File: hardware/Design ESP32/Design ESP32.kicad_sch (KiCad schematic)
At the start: 16 parts, among them J1 USB_C_Receptacle_USB2.0_16P, J2 Conn_01x08_Pin, U1 ESP32-S3-WROOM-1, U2 AMS1117-3.3

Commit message: edit skematik
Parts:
- added R5: R, symbol Device:R
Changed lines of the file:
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@@
+	(symbol
+		(lib_id "Device:R")
+		(at 57.15 109.22 0)
+		(unit 1)
+		(exclude_from_sim no)
+		(in_bom yes)
+		(on_board yes)
+		(dnp no)
+		(fields_autoplaced yes)
+		(property "Reference" "R5"
+			(at 59.69 107.9499 0)
+			(effects
+				(font
+					(size 1.27 1.27)
+				)
+				(justify left)
+			)
+		)
+		(property "Value" "R"
+			(at 59.69 110.4899 0)
+			(effects
+				(font
+					(size 1.27 1.27)
+				)
+				(justify left)
+			)
+		)
+		(property "Footprint" ""
+			(at 55.372 109.22 90)
+			(effects
+				(font
+					(size 1.27 1.27)
+				)
+				(hide yes)
+			)
+		)
+		(property "Datasheet" "~"
+			(at 57.15 109.22 0)
+			(effects
+				(font
+					(size 1.27 1.27)
+				)
+				(hide yes)
+			)
+		)
+		(property "Description" "Resistor"
+			(at 57.15 109.22 0)
+			(effects
+				(font
+					(size 1.27 1.27)
+				)
+				(hide yes)
+			)
+		)
+		(pin "1"
+		)
+		(pin "2"
+		)
+		(instances
+			(project ""
+				(path "/1962d16e-21fe-421b-a91f-5990a3b04182"
+					(reference "R5")
+					(unit 1)
+				)
+			)
+		)
+	)
 	(symbol
 		(lib_id "Device:R")

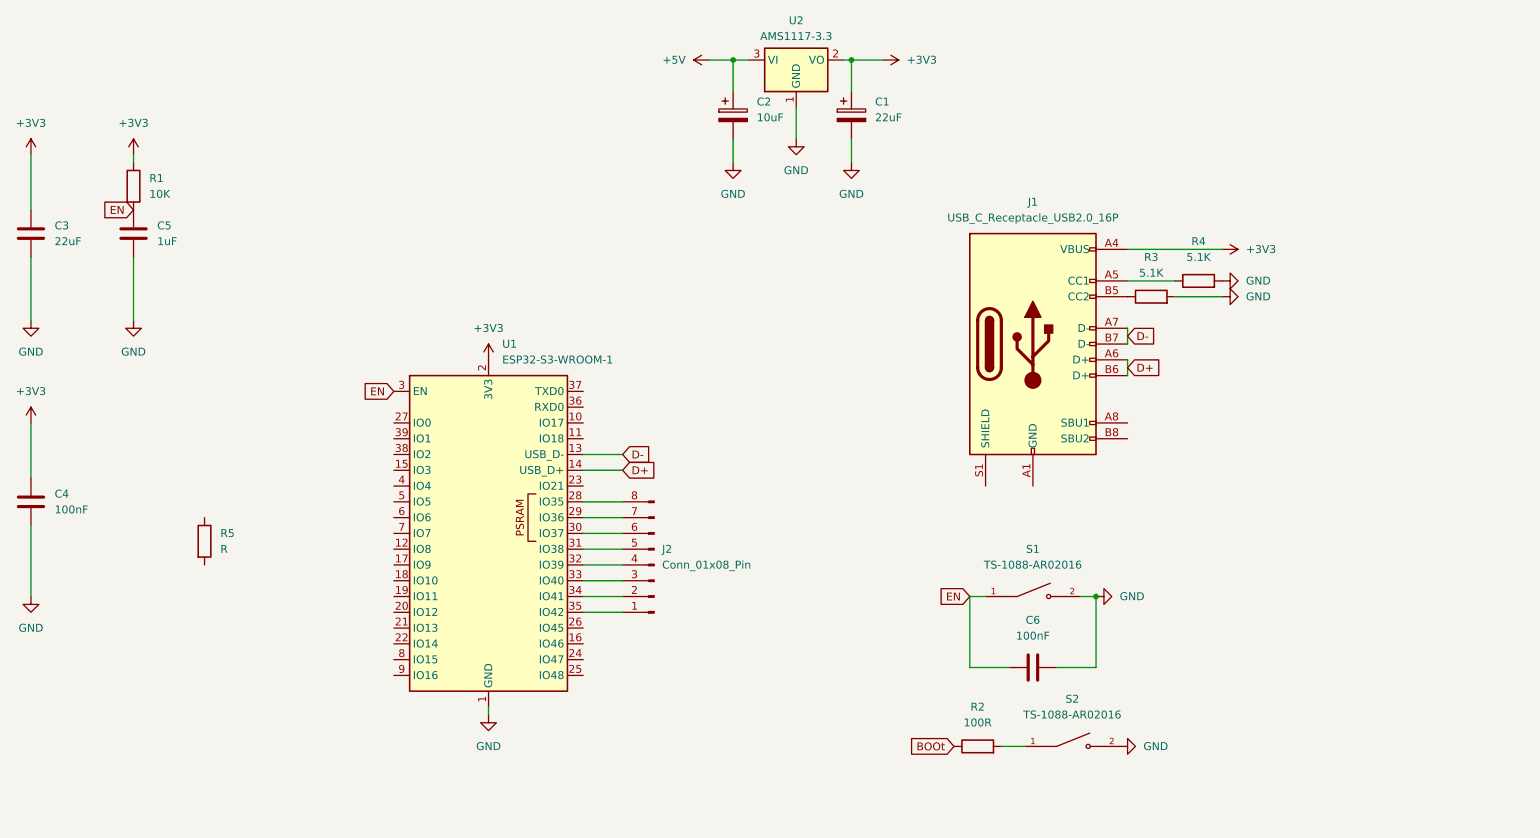
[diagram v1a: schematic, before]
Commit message: crosscheck schenmatic, progres track pcb
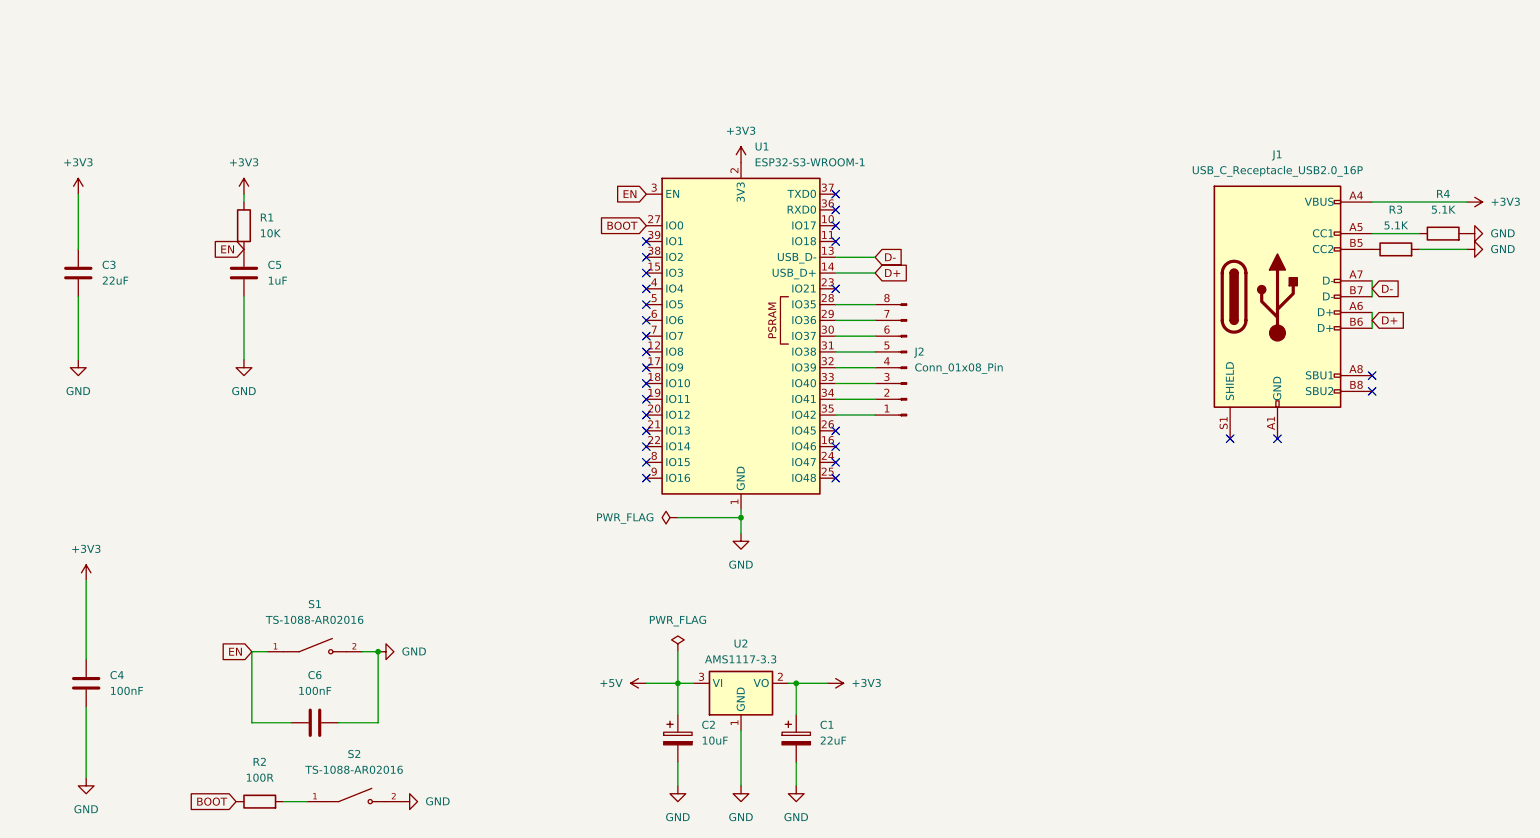
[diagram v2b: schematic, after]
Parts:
- removed R5: R, symbol Device:R
- C3, C4: footprint Capacitor_SMD:C_0805_2012Metric -> Capacitor_SMD:C_0603_1608Metric
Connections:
- net BOOt is gone; now on net BOOT: R2.1
- net BOOT: now reaches U1.27 (IO0)
- no-connect marks 0 -> 29
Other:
- moved on the sheet: C1, C2, C3, C4, C5, C6, J1, J2, R1, R2, R3, R4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

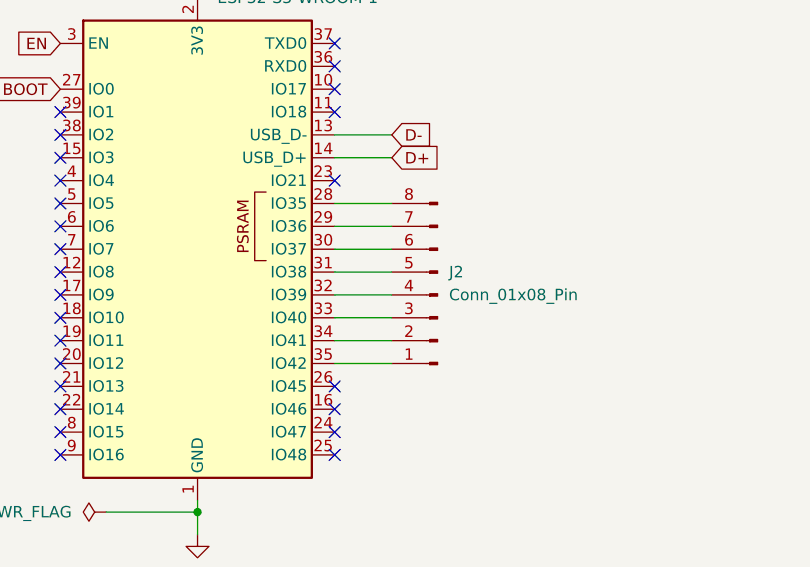
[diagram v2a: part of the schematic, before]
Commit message: jalur pcb, penanganan error 36 to 11
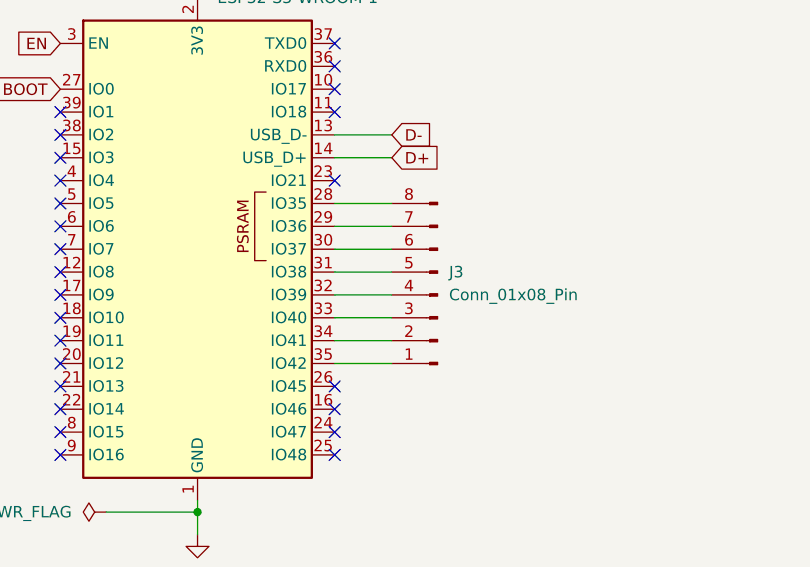
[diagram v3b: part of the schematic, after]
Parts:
- removed J2: Conn_01x08_Pin, Connector_PinHeader_1.00mm:PinHeader_1x08_P1.00mm_Vertical, symbol Connector:Conn_01x08_Pin
- added J3: Conn_01x08_Pin, Connector_PinHeader_1.00mm:PinHeader_1x08_P1.00mm_Vertical, symbol Connector:Conn_01x08_Pin
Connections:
- net at U1.35 (IO42): now also J3.1 (Pin_1)
- net at U1.34 (IO41): now also J3.2 (Pin_2)
- net at U1.33 (IO40): now also J3.3 (Pin_3)
- net at U1.32 (IO39): now also J3.4 (Pin_4)
- net at U1.31 (IO38): now also J3.5 (Pin_5)
- net at U1.30 (IO37): now also J3.6 (Pin_6)
- net at U1.29 (IO36): now also J3.7 (Pin_7)
- net at U1.28 (IO35): now also J3.8 (Pin_8)
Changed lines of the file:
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@@
-	(wire
-		(pts
-			(xy 165.1 86.36) (xy 158.75 86.36)
-		)
-		(stroke
-			(width 0)
-			(type default)
-		)
-	)
 	(wire
 		(pts
@@
 	(wire
 		(pts
+			(xy 158.75 88.9) (xy 165.1 88.9)
+		)
+		(stroke
+			(width 0)
+			(type default)
+		)
+	)
+	(wire
+		(pts
 			(xy 85.09 138.43) (xy 78.74 138.43)
 		)
@@
 	(wire
 		(pts
-			(xy 165.1 73.66) (xy 158.75 73.66)
+			(xy 158.75 73.66) (xy 165.1 73.66)
 		)
 		(stroke
@@
 	(wire
 		(pts
-			(xy 165.1 71.12) (xy 158.75 71.12)
-		)
-		(stroke
-			(width 0)
-			(type default)
-		)
-	)
-	(wire
-		(pts
 			(xy 143.51 139.7) (xy 143.51 148.59)
 		)
@@
 	(wire
 		(pts
+			(xy 158.75 76.2) (xy 165.1 76.2)
+		)
+		(stroke
+			(width 0)
+			(type default)
+		)
+	)
+	(wire
+		(pts
 			(xy 151.13 132.08) (xy 152.4 132.08)
 		)
@@
 	(wire
 		(pts
+			(xy 158.75 78.74) (xy 165.1 78.74)
+		)
+		(stroke
+			(width 0)
+			(type default)
+		)
+	)
+	(wire
+		(pts
 			(xy 38.1 147.32) (xy 38.1 135.89)
 		)
@@
 	(wire
 		(pts
-			(xy 165.1 81.28) (xy 158.75 81.28)
+			(xy 158.75 71.12) (xy 165.1 71.12)
 		)
 		(stroke
@@
 	(wire
 		(pts
+			(xy 158.75 83.82) (xy 165.1 83.82)
+		)
+		(stroke
+			(width 0)
+			(type default)
+		)
+	)
+	(wire
+		(pts
 			(xy 165.1 63.5) (xy 158.75 63.5)
 		)
@@
 	(wire
 		(pts
-			(xy 165.1 83.82) (xy 158.75 83.82)
-		)
-		(stroke
-			(width 0)
-			(type default)
-		)
-	)
-	(wire
-		(pts
 			(xy 67.31 127) (xy 64.77 127)
 		)
@@
 	(wire
 		(pts
-			(xy 165.1 88.9) (xy 158.75 88.9)
+			(xy 158.75 86.36) (xy 165.1 86.36)
+		)
+		(stroke
+			(width 0)
+			(type default)
+		)
+	)
+	(wire
+		(pts
+			(xy 158.75 81.28) (xy 165.1 81.28)
 		)
 		(stroke
@@
 		(pts
 			(xy 143.51 105.41) (xy 143.51 107.95)
-		)
-		(stroke
-			(width 0)
-			(type default)
-		)
-	)
-	(wire
-		(pts
-			(xy 165.1 78.74) (xy 158.75 78.74)
-		)
-		(stroke
-			(width 0)
-			(type default)
-		)
-	)
-	(wire
-		(pts
-			(xy 165.1 76.2) (xy 158.75 76.2)
 		)
 		(stroke
@@
 		(dnp no)
 		(fields_autoplaced yes)
-		(property "Reference" "J2"
+		(property "Reference" "J3"
 			(at 171.45 78.7399 0)
 			(effects
@@
 		)
 		(instances
-			(project ""
+			(project "Design ESP32"
 				(path "/1962d16e-21fe-421b-a91f-5990a3b04182"
-					(reference "J2")
+					(reference "J3")
 					(unit 1)
 				)

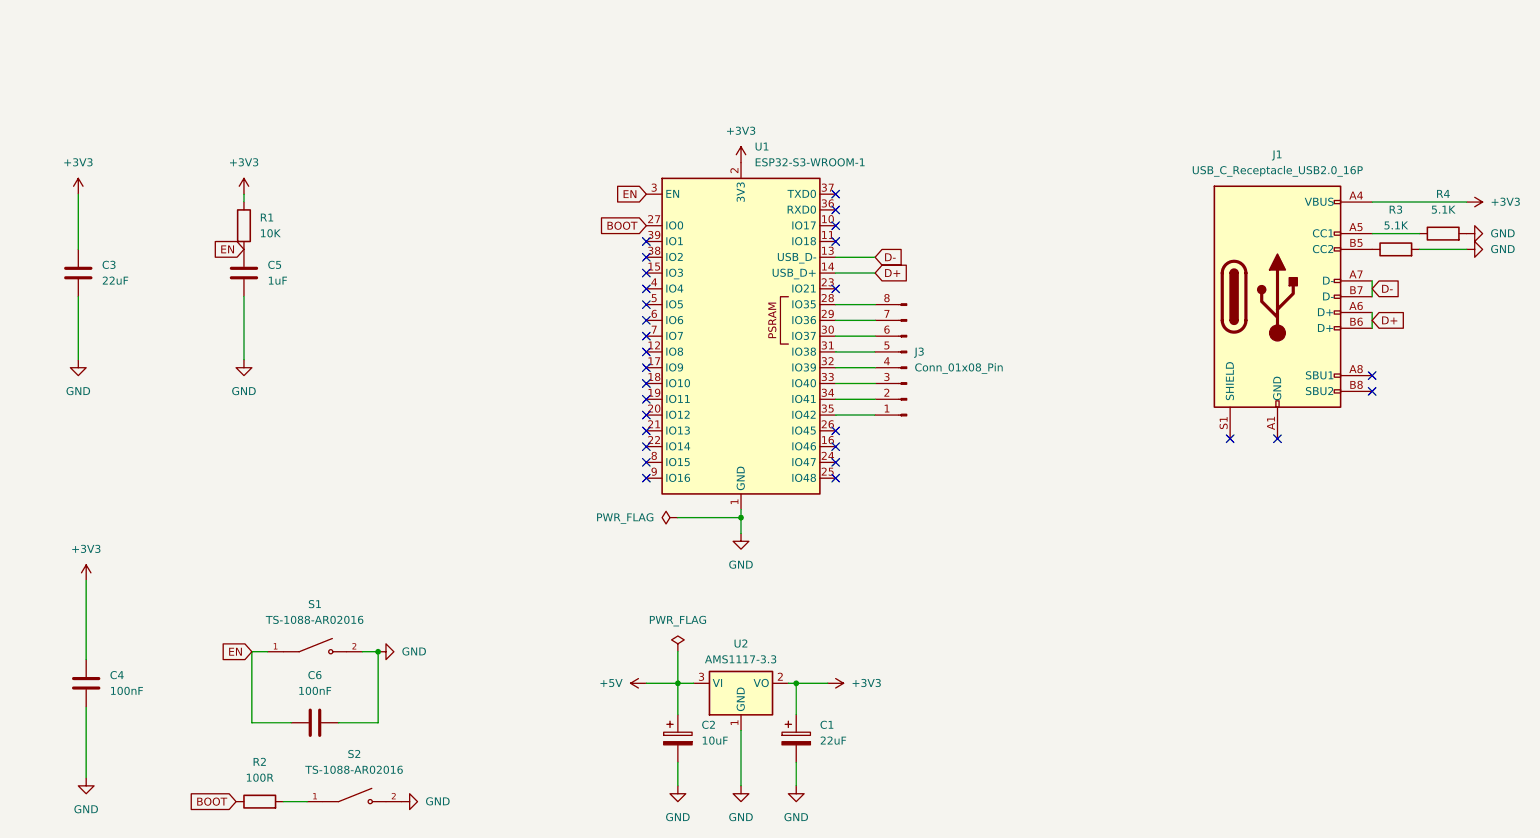
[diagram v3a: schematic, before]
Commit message: lanjut penanganan error dan penyelesaian design ESP32
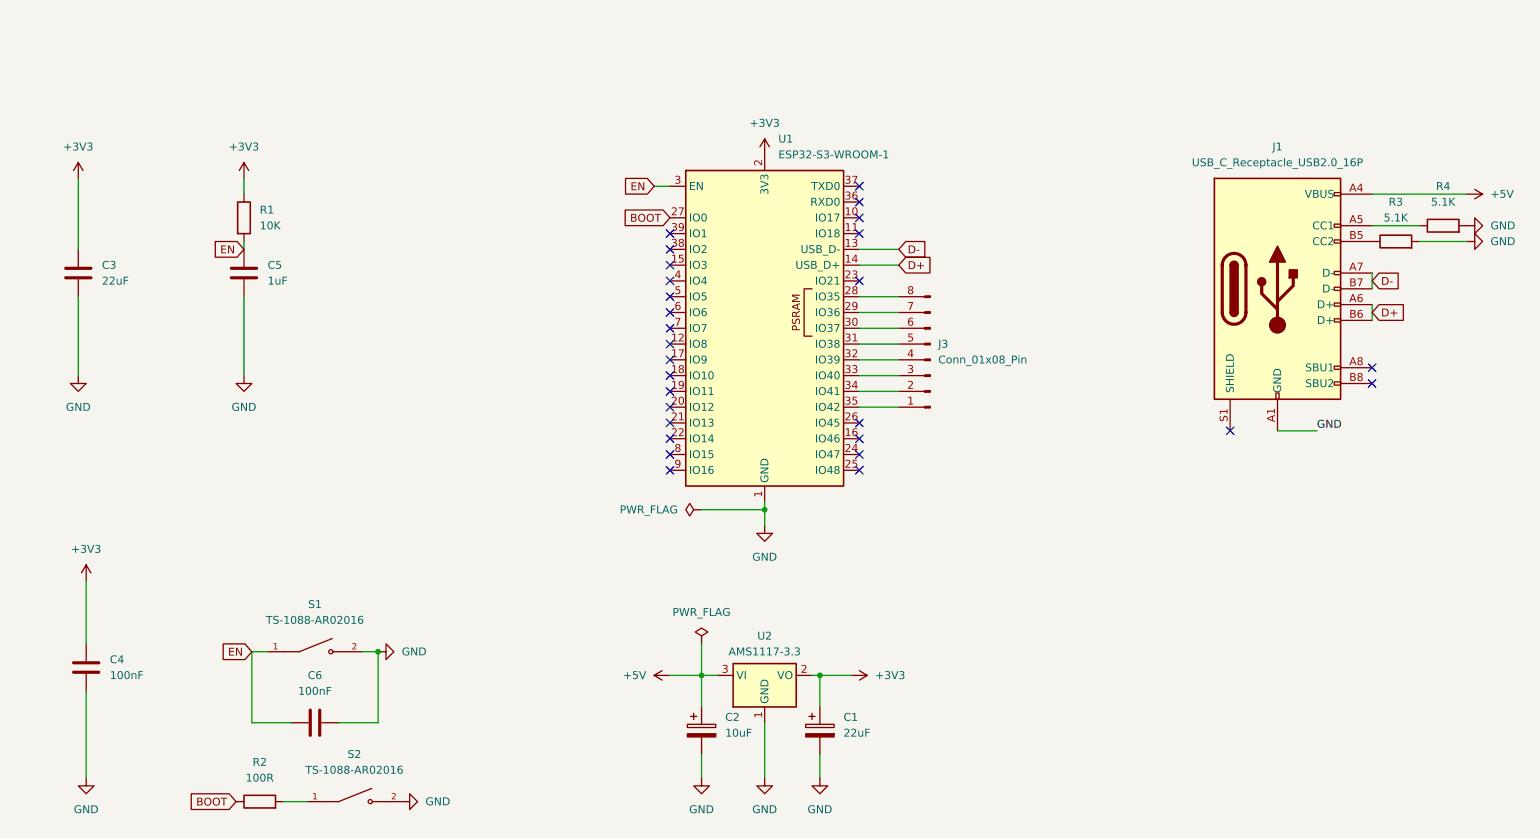
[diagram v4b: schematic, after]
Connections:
- net +3V3: no longer J1.A4 (VBUS), J1.A9 (VBUS), J1.B4 (VBUS), J1.B9 (VBUS)
- net +5V: now also J1.A4 (VBUS), J1.A9 (VBUS), J1.B4 (VBUS), J1.B9 (VBUS)
- net GND: now also J1.A1 (GND), J1.A12 (GND), J1.B1 (GND), J1.B12 (GND)
- no-connect marks 29 -> 28
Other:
- moved on the sheet: C1, C2, C4, J1, J3, R1, R3, R4, U1, U2

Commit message: update footprint C1, C2
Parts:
- C1: footprint Capacitor_SMD:C_0805_2012Metric -> Capacitor_Tantalum_SMD:CP_EIA-2012-15_AVX-P
- C2: footprint Capacitor_SMD:C_0805_2012Metric -> Capacitor_Tantalum_SMD:CP_EIA-1608-10_AVX-L
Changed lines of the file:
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@@
 			)
 		)
-		(property "Footprint" "Capacitor_SMD:C_0805_2012Metric"
+		(property "Footprint" "Capacitor_Tantalum_SMD:CP_EIA-1608-10_AVX-L"
 			(at 138.1252 143.51 0)
 			(effects
@@
 			)
 		)
-		(property "Footprint" "Capacitor_SMD:C_0805_2012Metric"
+		(property "Footprint" "Capacitor_Tantalum_SMD:CP_EIA-2012-15_AVX-P"
 			(at 157.1752 143.51 0)
 			(effects
